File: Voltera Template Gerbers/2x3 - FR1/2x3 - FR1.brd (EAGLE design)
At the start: 135 x 101.6 mm, 1 part

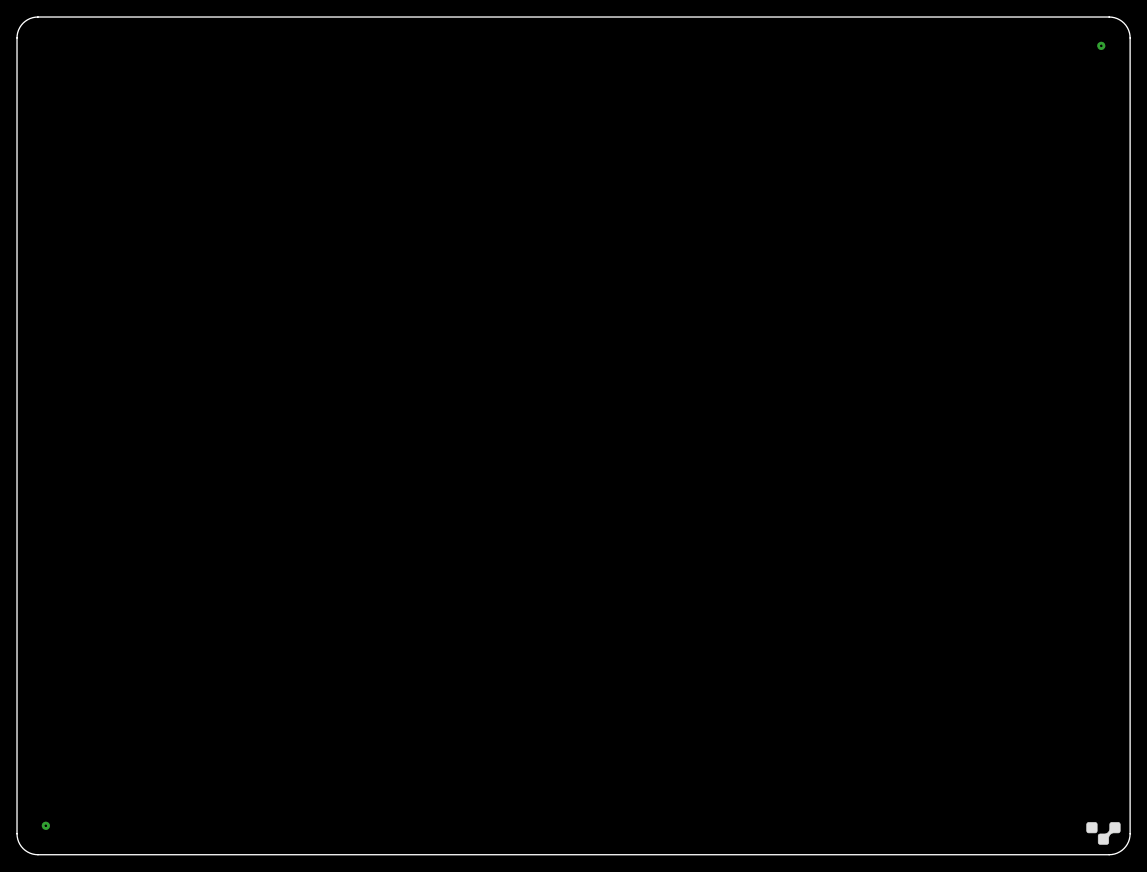
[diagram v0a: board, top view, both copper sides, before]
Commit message: Created 2x3 and 3x4 FR1 templates. Added 'fab' version of the templates
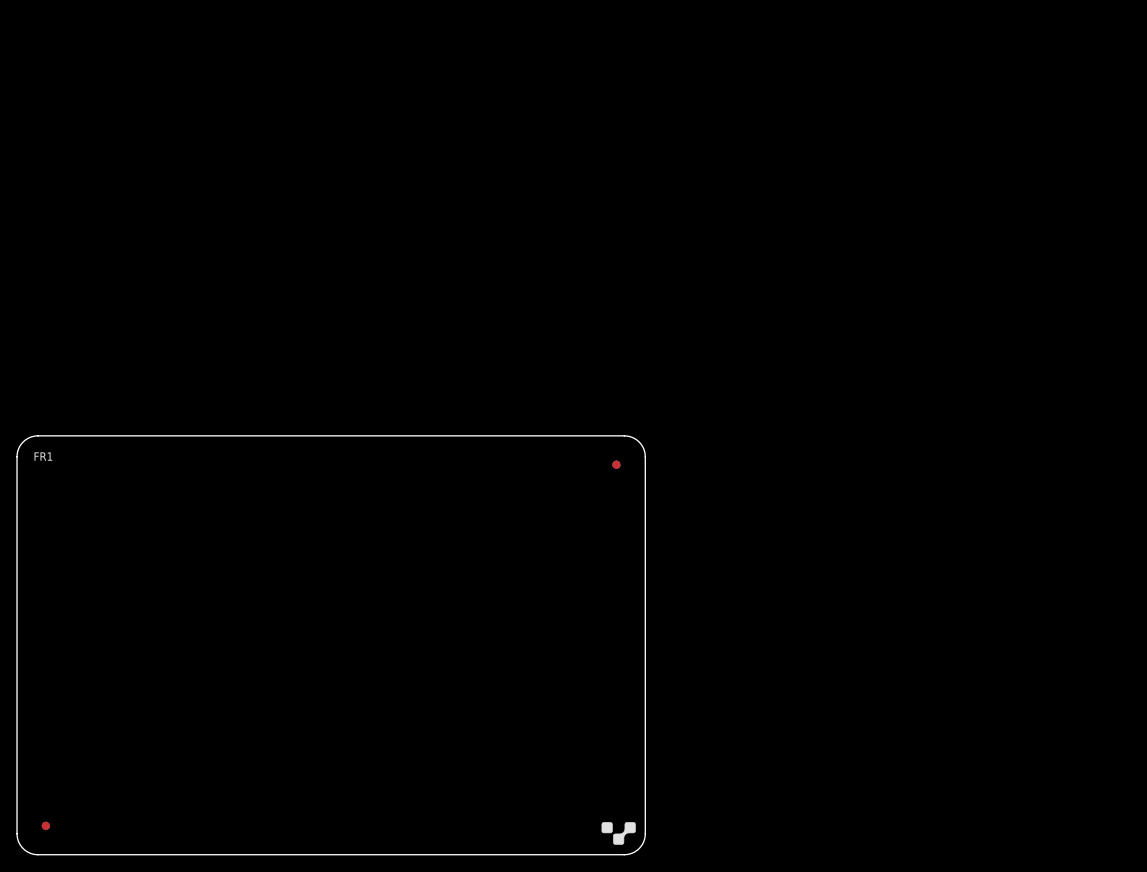
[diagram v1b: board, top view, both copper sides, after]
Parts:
- E$1: device voltera_community_lib:4X5_BOARD -> voltera_EAGLE_community_lib:2X3_BOARD_FR1
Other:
- board size 135 x 101.6 mm -> 76.2 x 50.8 mm
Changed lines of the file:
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@@
 <layer number="27" name="tValues" color="7" fill="1" visible="yes" active="yes"/>
 <layer number="28" name="bValues" color="7" fill="1" visible="yes" active="yes"/>
-<layer number="29" name="tStop" color="7" fill="3" visible="no" active="yes"/>
-<layer number="30" name="bStop" color="7" fill="6" visible="no" active="yes"/>
-<layer number="31" name="tCream" color="7" fill="4" visible="no" active="yes"/>
-<layer number="32" name="bCream" color="7" fill="5" visible="no" active="yes"/>
-<layer number="33" name="tFinish" color="6" fill="3" visible="no" active="yes"/>
-<layer number="34" name="bFinish" color="6" fill="6" visible="no" active="yes"/>
-<layer number="35" name="tGlue" color="7" fill="4" visible="no" active="yes"/>
-<layer number="36" name="bGlue" color="7" fill="5" visible="no" active="yes"/>
-<layer number="37" name="tTest" color="7" fill="1" visible="no" active="yes"/>
-<layer number="38" name="bTest" color="7" fill="1" visible="no" active="yes"/>
+<layer number="29" name="tStop" color="7" fill="3" visible="yes" active="yes"/>
+<layer number="30" name="bStop" color="7" fill="6" visible="yes" active="yes"/>
+<layer number="31" name="tCream" color="7" fill="4" visible="yes" active="yes"/>
+<layer number="32" name="bCream" color="7" fill="5" visible="yes" active="yes"/>
+<layer number="33" name="tFinish" color="6" fill="3" visible="yes" active="yes"/>
+<layer number="34" name="bFinish" color="6" fill="6" visible="yes" active="yes"/>
+<layer number="35" name="tGlue" color="7" fill="4" visible="yes" active="yes"/>
+<layer number="36" name="bGlue" color="7" fill="5" visible="yes" active="yes"/>
+<layer number="37" name="tTest" color="7" fill="1" visible="yes" active="yes"/>
+<layer number="38" name="bTest" color="7" fill="1" visible="yes" active="yes"/>
 <layer number="39" name="tKeepout" color="4" fill="11" visible="yes" active="yes"/>
 <layer number="40" name="bKeepout" color="1" fill="11" visible="yes" active="yes"/>
@@
 <layer number="42" name="bRestrict" color="1" fill="10" visible="yes" active="yes"/>
 <layer number="43" name="vRestrict" color="2" fill="10" visible="yes" active="yes"/>
-<layer number="44" name="Drills" color="7" fill="1" visible="no" active="yes"/>
-<layer number="45" name="Holes" color="7" fill="1" visible="no" active="yes"/>
-<layer number="46" name="Milling" color="3" fill="1" visible="no" active="yes"/>
+<layer number="44" name="Drills" color="7" fill="1" visible="yes" active="yes"/>
+<layer number="45" name="Holes" color="7" fill="1" visible="yes" active="yes"/>
+<layer number="46" name="Milling" color="3" fill="1" visible="yes" active="yes"/>
 <layer number="47" name="Measures" color="7" fill="1" visible="yes" active="yes"/>
 <layer number="48" name="Document" color="7" fill="1" visible="yes" active="yes"/>
@@
 <layer number="112" name="tSilk" color="7" fill="1" visible="yes" active="yes"/>
 <layer number="113" name="IDFDebug" color="4" fill="1" visible="yes" active="yes"/>
+<layer number="114" name="Badge_Outline" color="7" fill="1" visible="yes" active="yes"/>
+<layer number="115" name="ReferenceISLANDS" color="7" fill="1" visible="yes" active="yes"/>
 <layer number="116" name="Patch_BOT" color="9" fill="4" visible="yes" active="yes"/>
 <layer number="118" name="Rect_Pads" color="7" fill="1" visible="no" active="no"/>
@@
 <layer number="223" name="223bmp" color="24" fill="1" visible="no" active="no"/>
 <layer number="224" name="224bmp" color="25" fill="1" visible="no" active="no"/>
+<layer number="225" name="225bmp" color="7" fill="1" visible="yes" active="yes"/>
+<layer number="226" name="226bmp" color="7" fill="1" visible="yes" active="yes"/>
+<layer number="227" name="227bmp" color="7" fill="1" visible="yes" active="yes"/>
+<layer number="228" name="228bmp" color="7" fill="1" visible="yes" active="yes"/>
+<layer number="229" name="229bmp" color="7" fill="1" visible="yes" active="yes"/>
+<layer number="230" name="230bmp" color="7" fill="1" visible="yes" active="yes"/>
 <layer number="231" name="Eagle3D_PG1" color="7" fill="1" visible="no" active="no"/>
 <layer number="232" name="Eagle3D_PG2" color="7" fill="1" visible="no" active="no"/>
@@
 <layer number="251" name="SMDround" color="12" fill="11" visible="no" active="no"/>
 <layer number="254" name="cooling" color="7" fill="1" visible="yes" active="yes"/>
+<layer number="255" name="routoute" color="7" fill="1" visible="yes" active="yes"/>
 </layers>
 <board>
 <plain>
-<dimension x1="0" y1="3" x2="135" y2="3" x3="67.5" y3="-13" textsize="1.778" layer="47"/>
-<dimension x1="0" y1="0" x2="0" y2="101.6" x3="-4.8" y3="50.8" textsize="1.778" layer="47"/>
 </plain>
 <attributes>
@@
 </autorouter>
 <elements>
-<element name="E$1" library="voltera_community_lib" package="4X5_BOARD" value="" x="0" y="0"/>
+<element name="E$1" library="voltera_EAGLE_community_lib" package="2X3_BOARD_FR1" value="" x="0" y="0"/>
 </elements>
 <signals>
